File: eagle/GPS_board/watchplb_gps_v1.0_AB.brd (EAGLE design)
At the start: 50.2 x 50 mm, 10 parts, among them IC1 SAM-M8Q

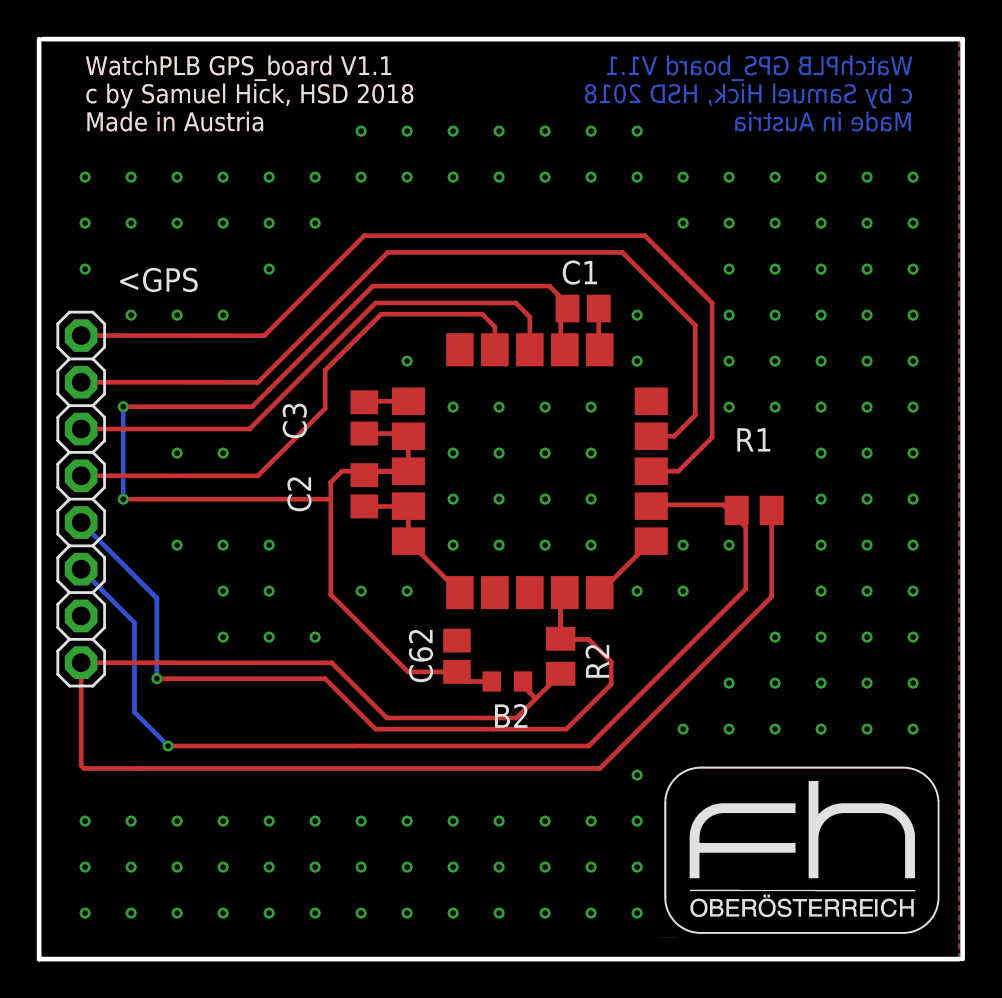
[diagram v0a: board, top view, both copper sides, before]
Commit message: von Armin überarbeitete Version der GPS-Platine
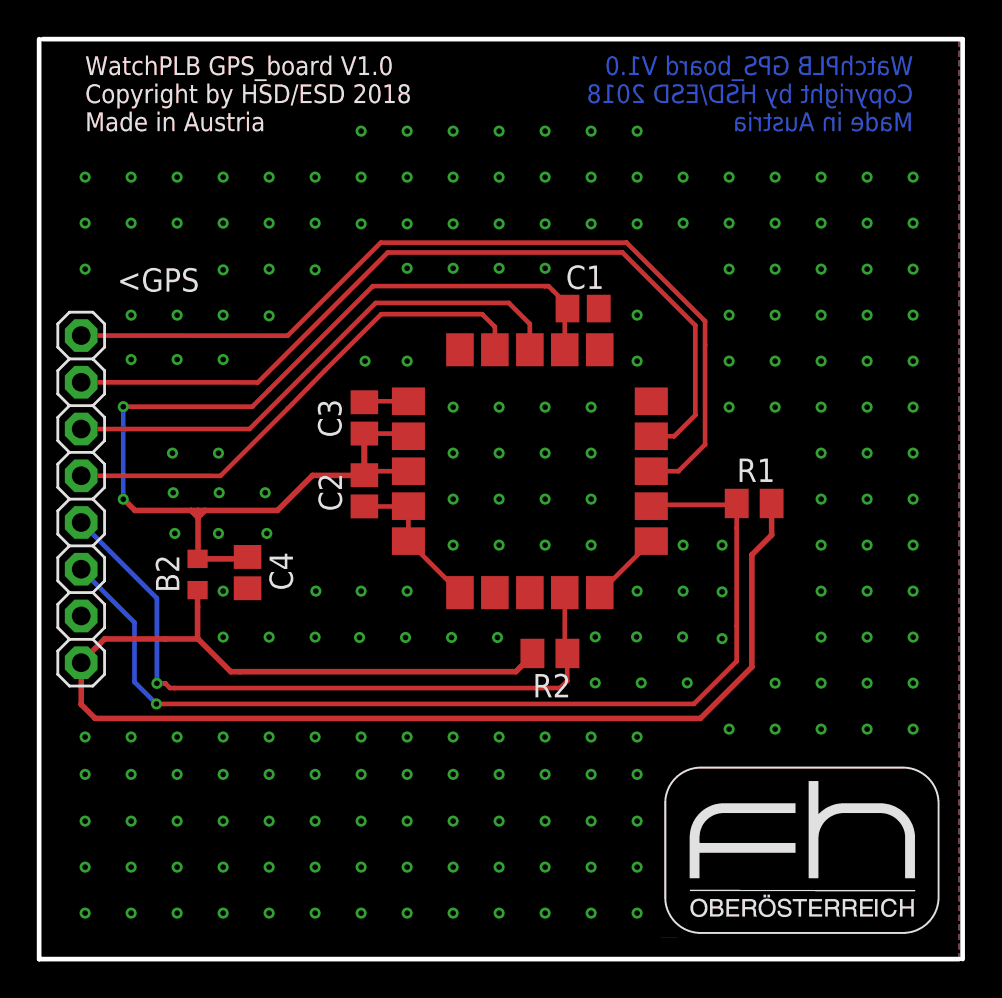
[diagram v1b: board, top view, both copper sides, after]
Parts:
- removed C62: 4.7uF, resistor:C0805
- added C4: 4.7uF, resistor:C0805
- moved B2 17.8 mm to (8.61, 20.9), turned to 90 degrees
- moved R2 0.60 mm to (27.8, 16.6), turned to 0 degrees
- moved R1 0.38 mm to (38.9, 24.8)
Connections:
- net GND: now also C4.2; no longer C62.2
- net N$79: now also C4.1; no longer C62.1
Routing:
- net N$79: track 74.4 -> 65.3 mm
- net GPS_SDA: track 46.6 -> 37.9 mm
- net +3V3: track 81.4 -> 78.5 mm
- net GND: track 17.1 -> 14.8 mm, vias 165 -> 220
- net GPS_TXD: track 49.4 -> 48.0 mm
- net GPS_EXTINT: track 28.9 -> 27.7 mm
- net GPS_SCL: track 56.1 -> 55.0 mm
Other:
- board text added: "WatchPLB GPS_board V1.0 Copyright by HSD/ESD 2018 Made in Austria"

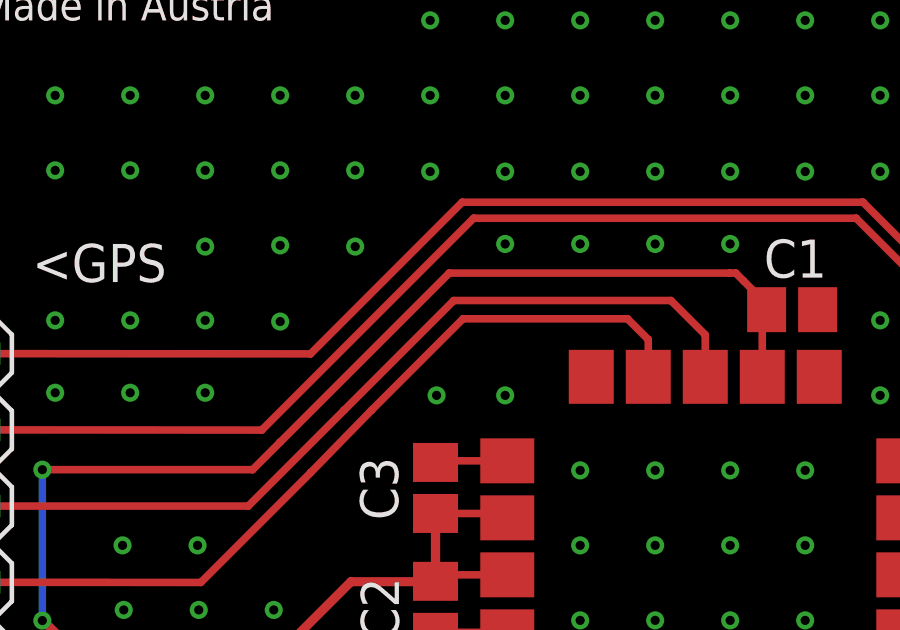
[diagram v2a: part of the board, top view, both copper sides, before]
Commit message: einige kleine Änderungen: mcp111 ist smd massen verbinden taster footprint richtig orientierungspunkt U5 BQ ding richtungsmarkierung bei diode im Bat prot reset leitung bei pin verbinden LED rs auf 470R Charger SS pin mit pullup damits ohne firmware geht beschriftung am programmierheader verrutscht positiv beschriftung akkustecker usb 5v der unteren beiden trennen
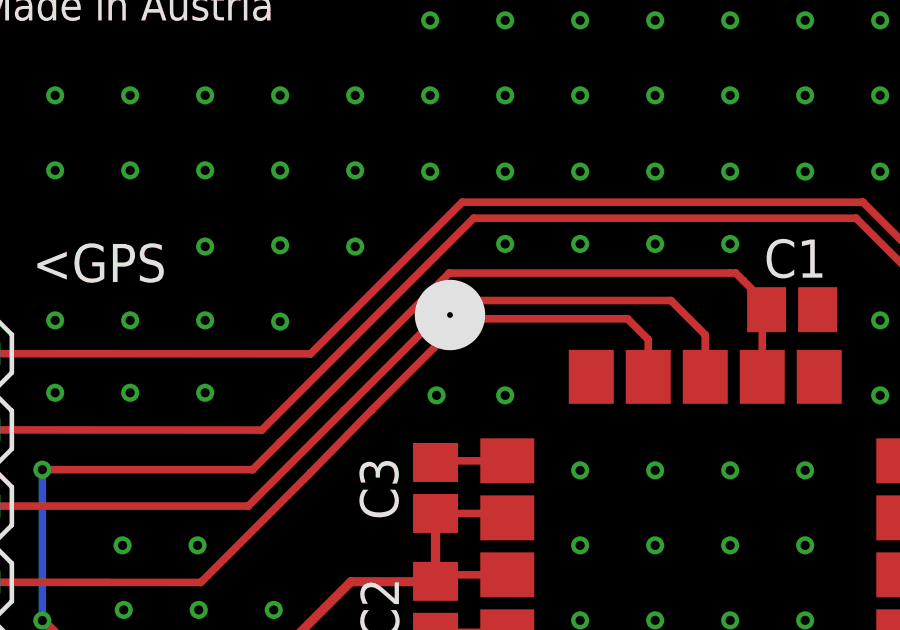
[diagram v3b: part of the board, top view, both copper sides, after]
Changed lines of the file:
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@@
 <layer number="20" name="Dimension" color="15" fill="1" visible="yes" active="yes"/>
 <layer number="21" name="tPlace" color="7" fill="1" visible="yes" active="yes"/>
-<layer number="22" name="bPlace" color="7" fill="1" visible="no" active="yes"/>
+<layer number="22" name="bPlace" color="7" fill="1" visible="yes" active="yes"/>
 <layer number="23" name="tOrigins" color="15" fill="1" visible="yes" active="yes"/>
-<layer number="24" name="bOrigins" color="15" fill="1" visible="no" active="yes"/>
+<layer number="24" name="bOrigins" color="15" fill="1" visible="yes" active="yes"/>
 <layer number="25" name="tNames" color="7" fill="1" visible="yes" active="yes"/>
 <layer number="26" name="bNames" color="7" fill="1" visible="yes" active="yes"/>
@@
 <wire x1="0" y1="50" x2="0" y2="0" width="0.254" layer="20"/>
 <wire x1="0" y1="0" x2="50" y2="0" width="0.254" layer="20"/>
+<circle x="18.161" y="35.179" radius="0.5388125" width="1.27" layer="25"/>
 </plain>
 <attributes>
